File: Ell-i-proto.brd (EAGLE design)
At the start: 99 x 53.3 mm, 148 parts, among them J10 KLDX-SMT2-0202, J2 PWMH, J3 PWR, J4 PWML, J5 ANAL, J6 SPI, J7 COMM, J8 ANAH, J9 RJ45, Q1 FDV304P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

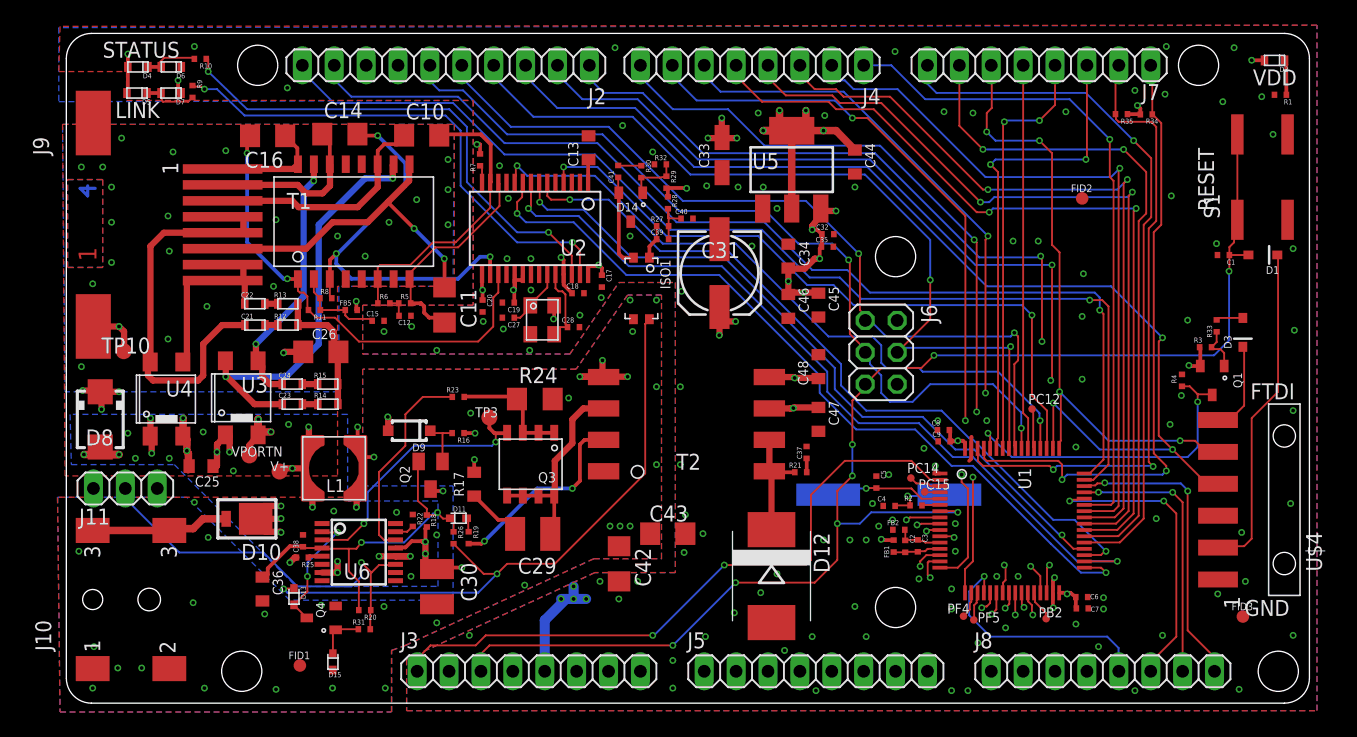
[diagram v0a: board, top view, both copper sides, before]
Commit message: Comments and limitations from PV and PNR applied, generic clearances increased to 0.2mm
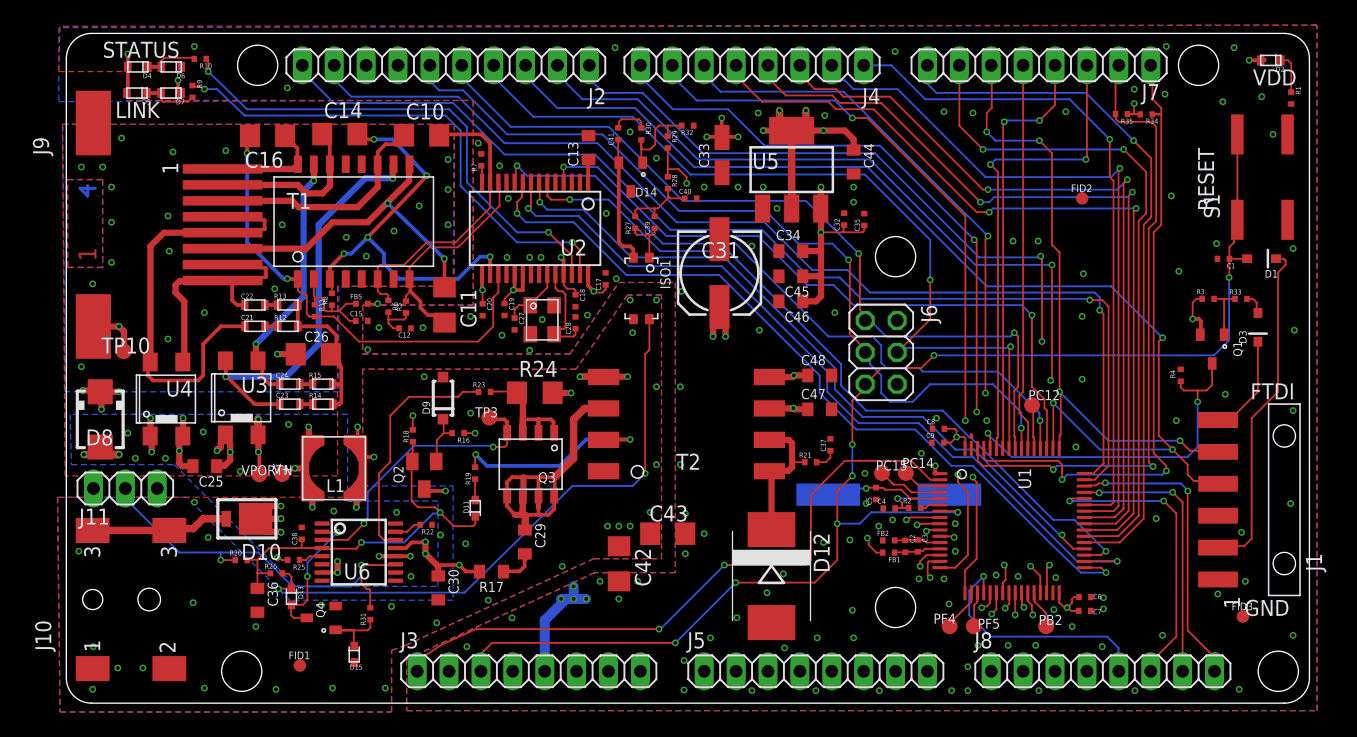
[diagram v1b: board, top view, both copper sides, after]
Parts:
- C29, C30: device rcl:C1210 -> ell-i:0805
- PB2, PC12, PC14, PC15, PF4, PF5: value TPTP06R -> TPSB1,27; device testpad:TP06R -> testpad:B1,27
- moved R26 14.4 mm to (16.7, 10.3), turned to 0 degrees
- moved R20 10.6 mm to (13.9, 11.4), turned to 0 degrees
- moved R17 7.10 mm to (33.9, 10.5), turned to 180 degrees
- moved R18 6.87 mm to (27.6, 21.3), turned to 270 degrees
- moved R19 5.17 mm to (32.6, 18.3), turned to 90 degrees
- moved R3 3.86 mm to (90.9, 32.2)
- moved R32 3.77 mm to (49.5, 46.0), turned to 0 degrees
- moved D9 3.73 mm to (30.0, 24.3), turned to 90 degrees
- moved PC15 3.72 mm to (65.0, 18.3)
- moved C35 3.65 mm to (63.5, 38.5), turned to 90 degrees
- moved R29 3.20 mm to (47.9, 44.7)
- moved C45 3.18 mm to (57.7, 34.0), turned to 180 degrees
- moved C41 3.00 mm to (44.0, 45.4)
- moved R30 3.00 mm to (45.8, 45.3)
- moved R33 2.89 mm to (93.5, 32.2), turned to 0 degrees
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- renumbered U$4 to J1
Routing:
- net N27571: track 16.7 -> 31.7 mm
- net +3V3: track 55.6 -> 63.6 mm
- net N40137: track 7.38 -> 14.7 mm
- net RJ45-7-8: track 16.1 -> 22.6 mm
- net +5V: track 41.6 -> 47.6 mm, vias 14 -> 11
- net GNDI: track 7.62 -> 1.89 mm, vias 113 -> 121
- net N40108: track 4.19 -> 8.33 mm
- net N$3: track 1.23 -> 5.24 mm
- net N27735: track 9.67 -> 13.4 mm
- net N13468: track 6.18 -> 9.54 mm
- net N40361: track 9.28 -> 12.2 mm
- net N28455: track 16.3 -> 19.2 mm
- net RJ45-4-5: track 32.4 -> 35.1 mm
- net N22914: track 10.7 -> 13.3 mm
- net N118561: track 26.1 -> 28.7 mm
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
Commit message: plane optimizations, diode marks & pin1:s to tsilk, jumpers named
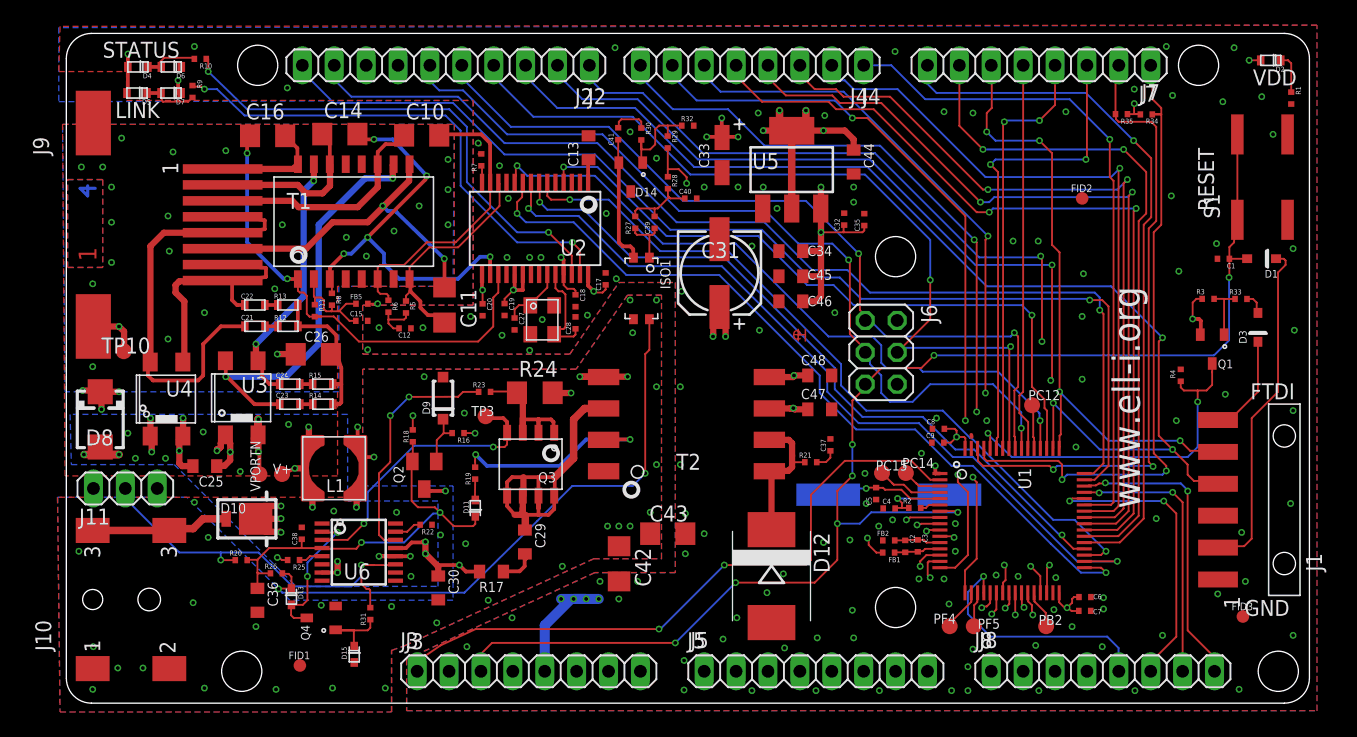
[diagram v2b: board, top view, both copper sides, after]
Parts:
- added U$4: (no value), hapines:EH-LOGO
- moved TP3 0.32 mm to (33.4, 22.9)
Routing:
- net +5V: track 47.6 -> 50.3 mm
- net RJ45-6: track 27.2 -> 27.8 mm
- net +3V3: track 63.6 -> 63.0 mm
- net N28455: vias 0 -> 2
- net GNDI: vias 121 -> 120
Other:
- board text added: "J2"
- board text added: "J3"
- board text added: "J4"
- board text added: "J5"
- board text added: "J7"
- board text added: "J8"
- board text added: "www.ell-i.org"
